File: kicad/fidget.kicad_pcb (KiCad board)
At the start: 2 copper layers, 74 x 38.9 mm, 13 parts, among them SW1 SW_Push, SW2 SW_Push, SW3 SW_Push, SW4 SW_Push, U1 XIAO-RP2040-DIP

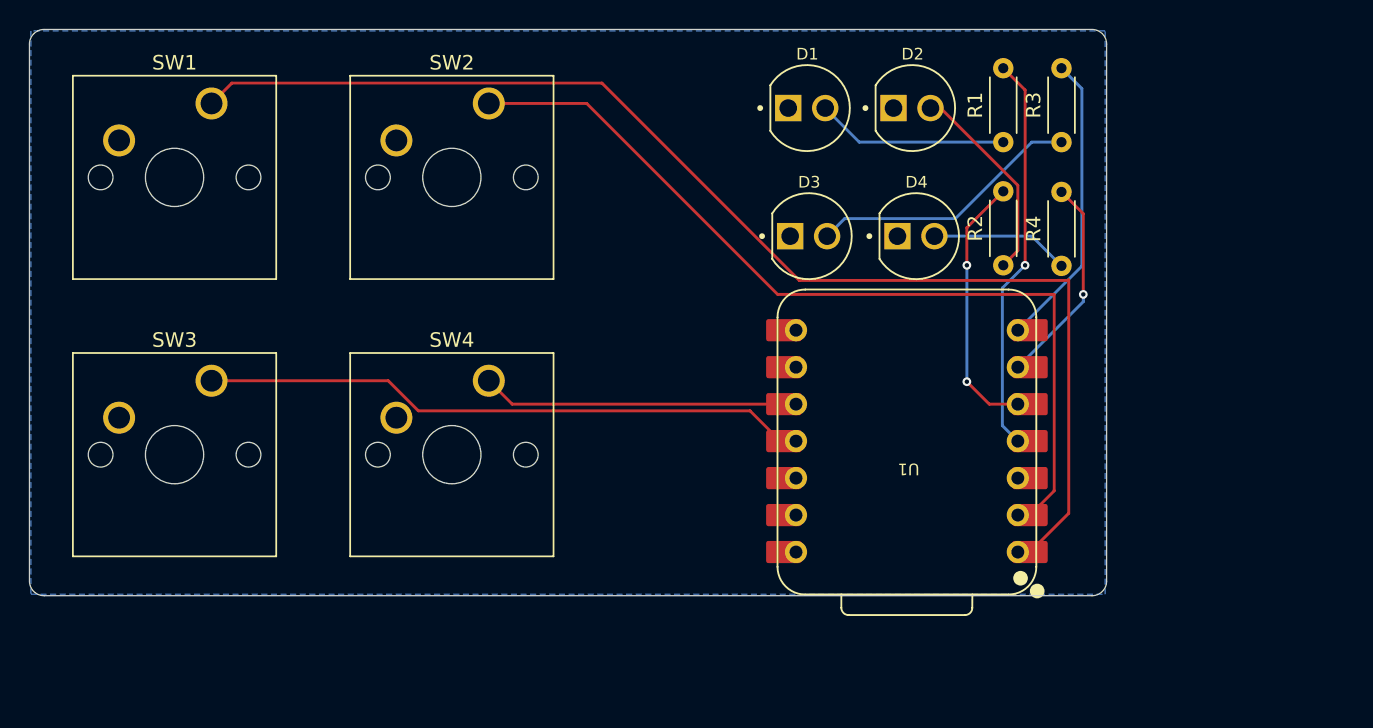
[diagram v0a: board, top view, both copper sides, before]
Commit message: update silkscreen + images
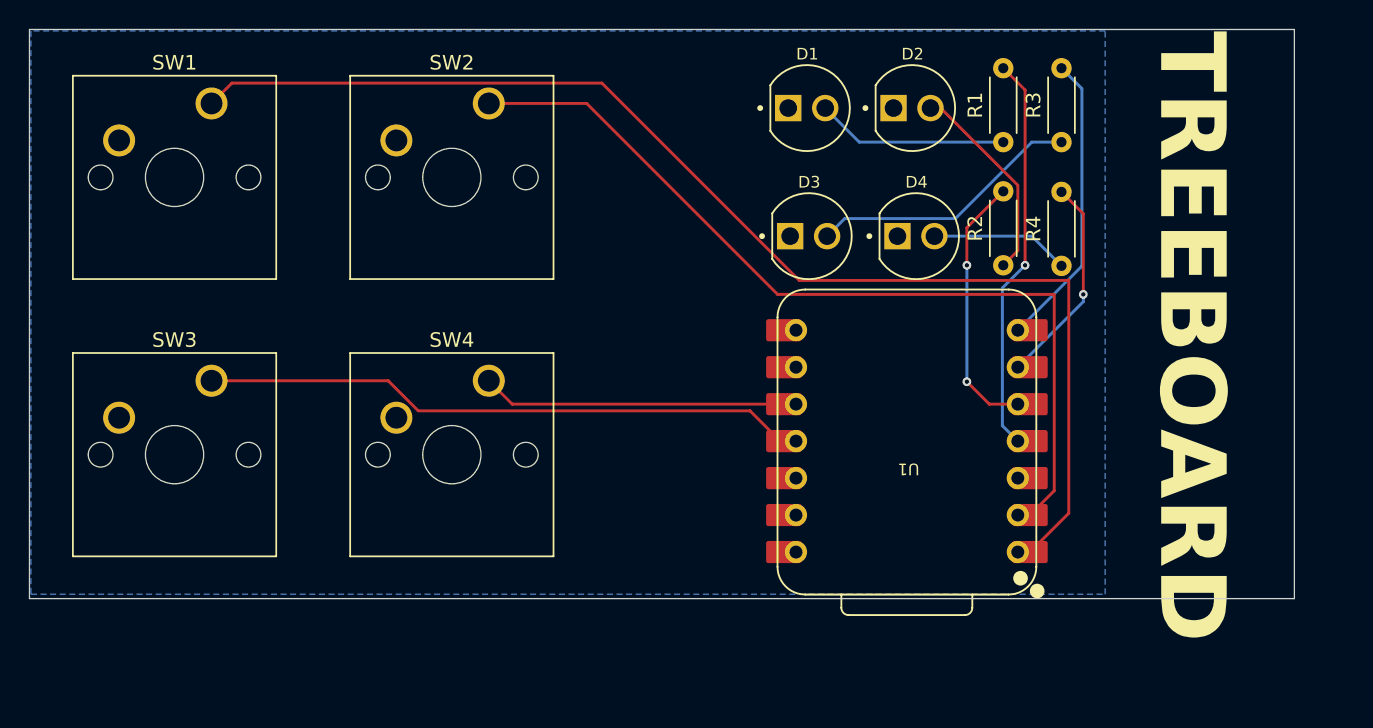
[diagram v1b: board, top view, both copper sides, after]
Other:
- board size 74 x 38.9 mm -> 86.9 x 39.1 mm
- board text added: "Duel"
- board text added: "GAMES"
- board text added: "Memory Game"
- board text added: "Reaction Tester"
- board text added: "TREEBOARD"
- board text added: "go to https://github.com/DaBlower/treeboard to view instructions"
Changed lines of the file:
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@@
 		)
 	)
-	(gr_arc
-		(start 85.6 71.8)
-		(mid 85.892893 71.092893)
-		(end 86.6 70.8)
+	(gr_rect
+		(start 85.6 70.8)
+		(end 172.5 109.9)
 		(stroke
 			(width 0.05)
 			(type default)
 		)
+		(fill none)
 		(layer "Edge.Cuts")
 	)
-	(gr_line
-		(start 158.6 109.7)
-		(end 86.6 109.7)
-		(stroke
-			(width 0.05)
-			(type default)
+	(gr_text "Reaction Tester"
+		(at 132.3 107.8 270)
+		(layer "B.SilkS")
+		(effects
+			(font
+				(size 3 3)
+				(thickness 0.6)
+				(bold yes)
+			)
+			(justify left bottom mirror)
 		)
-		(layer "Edge.Cuts")
 	)
-	(gr_arc
-		(start 159.6 108.7)
-		(mid 159.307107 109.407107)
-		(end 158.6 109.7)
-		(stroke
-			(width 0.05)
-			(type default)
+	(gr_text "Duel"
+		(at 128.2 107.8 270)
+		(layer "B.SilkS")
+		(effects
+			(font
+				(size 3 3)
+				(thickness 0.6)
+				(bold yes)
+			)
+			(justify left bottom mirror)
 		)
-		(layer "Edge.Cuts")
 	)
-	(gr_arc
-		(start 158.6 70.8)
-		(mid 159.307107 71.092893)
-		(end 159.6 71.8)
-		(stroke
-			(width 0.05)
-			(type default)
+	(gr_text "GAMES"
+		(at 161.4 108.5 270)
+		(layer "B.SilkS")
+		(effects
+			(font
+				(size 7 7)
+				(thickness 1.75)
+				(bold yes)
+			)
+			(justify left bottom mirror)
 		)
-		(layer "Edge.Cuts")
 	)
-	(gr_line
-		(start 159.6 71.8)
-		(end 159.6 108.7)
-		(stroke
-			(width 0.05)
-			(type default)
+	(gr_text "go to\nhttps://github.com/DaBlower/treeboard\nto view instructions"
+		(at 103.3 106.4 270)
+		(layer "B.SilkS")
+		(effects
+			(font
+				(size 1 1)
+				(thickness 0.2)
+				(bold yes)
+			)
+			(justify left bottom mirror)
 		)
-		(layer "Edge.Cuts")
 	)
-	(gr_line
-		(start 86.6 70.8)
-		(end 158.6 70.8)
-		(stroke
-			(width 0.05)
-			(type default)
+	(gr_text "Memory Game"
+		(at 124.2 107.8 270)
+		(layer "B.SilkS")
+		(effects
+			(font
+				(size 3 3)
+				(thickness 0.6)
+				(bold yes)
+			)
+			(justify left bottom mirror)
 		)
-		(layer "Edge.Cuts")
 	)
-	(gr_line
-		(start 85.6 108.7)
-		(end 85.6 71.8)
-		(stroke
-			(width 0.05)
-			(type default)
+	(gr_text "TREEBOARD"
+		(at 162.8 70.9 270)
+		(layer "F.SilkS")
+		(effects
+			(font
+				(size 4.5 4.5)
+				(thickness 1.125)
+				(bold yes)
+			)
+			(justify left bottom)
 		)
-		(layer "Edge.Cuts")
-	)
-	(gr_arc
-		(start 86.6 109.7)
-		(mid 85.892893 109.407107)
-		(end 85.6 108.7)
-		(stroke
-			(width 0.05)
-			(type default)
-		)
-		(layer "Edge.Cuts")
 	)
 	(segment

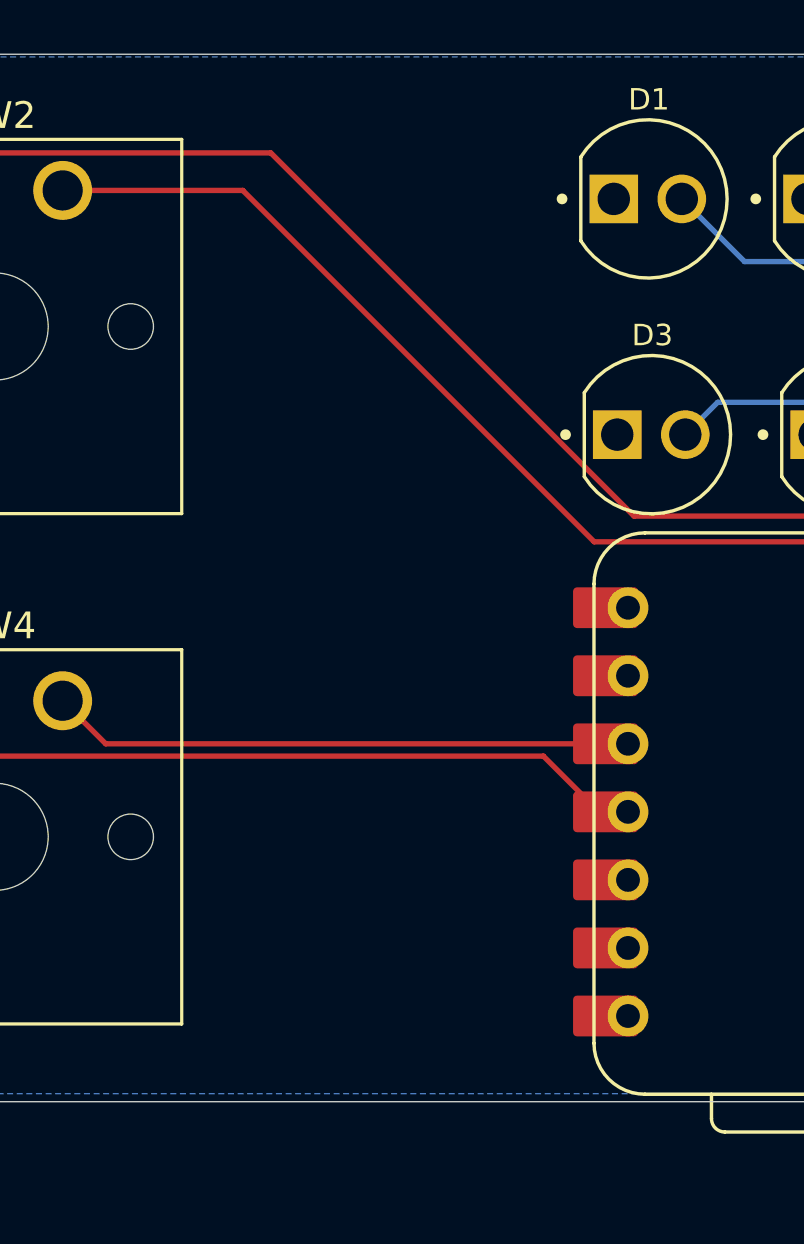
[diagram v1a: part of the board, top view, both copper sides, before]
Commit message: add more silkscreen
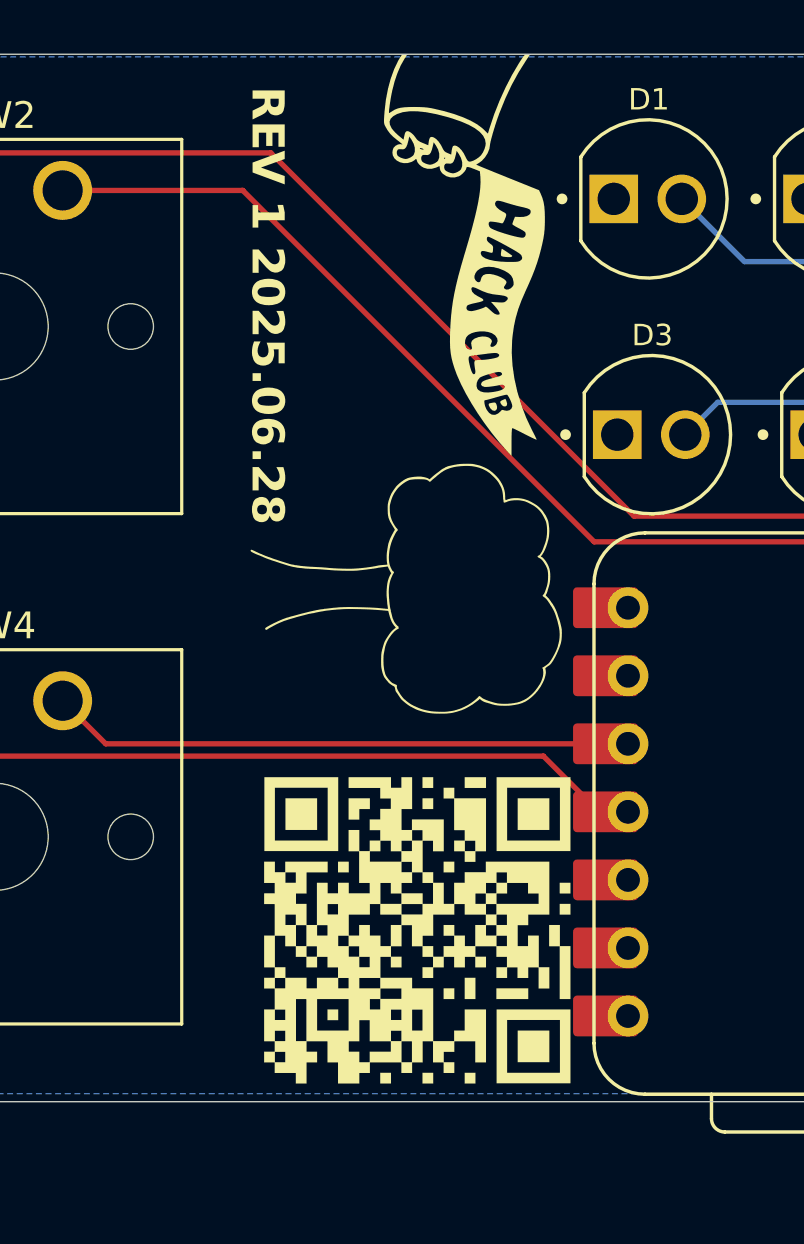
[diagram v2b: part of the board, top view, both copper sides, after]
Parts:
- added G***: LOGO, LOGO, F.Cu at (132.2, 78.3)
- added G***: LOGO, LOGO, F.Cu at (129.8, 90.9)
- added G***: LOGO, LOGO, F.Cu at (130.4, 103.5)
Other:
- board text added: "REV 1 2025.06.28"

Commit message: add keychain hole
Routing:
- net (no net): vias 0 -> 1
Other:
- board size 86.9 x 39.1 mm -> 90.3 x 39.1 mm
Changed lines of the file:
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@@
 			(plot_on_all_layers_selection 0x0000000_00000000)
 			(disableapertmacros no)
-			(usegerberextensions no)
+			(usegerberextensions yes)
 			(usegerberattributes yes)
 			(usegerberadvancedattributes yes)
@@
 			(plotinvisibletext no)
 			(sketchpadsonfab no)
-			(subtractmaskfromsilk no)
+			(subtractmaskfromsilk yes)
 			(outputformat 1)
 			(mirror no)
-			(drillshape 1)
+			(drillshape 0)
 			(scaleselection 1)
-			(outputdirectory "")
+			(outputdirectory "production/")
 		)
 	)
@@
 		)
 	)
-	(gr_rect
-		(start 85.6 70.8)
-		(end 172.5 109.9)
+	(gr_arc
+		(start 174.9 70.8)
+		(mid 175.607107 71.092893)
+		(end 175.9 71.8)
+		(stroke
+			(width 0.05)
+			(type default)
+		)
+		(layer "Edge.Cuts")
+	)
+	(gr_line
+		(start 175.334394 78.239173)
+		(end 170.565606 84.860827)
+		(stroke
+			(width 0.05)
+			(type default)
+		)
+		(layer "Edge.Cuts")
+	)
+	(gr_line
+		(start 169 109.9)
+		(end 148.4 109.9)
+		(stroke
+			(width 0.05)
+			(type default)
+		)
+		(layer "Edge.Cuts")
+	)
+	(gr_arc
+		(start 170 86.614031)
+		(mid 170.144901 85.69294)
+		(end 170.565606 84.860827)
+		(stroke
+			(width 0.05)
+			(type default)
+		)
+		(layer "Edge.Cuts")
+	)
+	(gr_arc
+		(start 175.9 76.485969)
+		(mid 175.755099 77.40706)
+		(end 175.334394 78.239173)
+		(stroke
+			(width 0.05)
+			(type default)
+		)
+		(layer "Edge.Cuts")
+	)
+	(gr_line
+		(start 148.4 109.9)
+		(end 86.6 109.9)
+		(stroke
+			(width 0.05)
+			(type default)
+		)
+		(layer "Edge.Cuts")
+	)
+	(gr_line
+		(start 175.9 71.8)
+		(end 175.9 76.485969)
+		(stroke
+			(width 0.05)
+			(type default)
+		)
+		(layer "Edge.Cuts")
+	)
+	(gr_arc
+		(start 86.6 109.9)
+		(mid 85.892893 109.607107)
+		(end 85.6 108.9)
+		(stroke
+			(width 0.05)
+			(type default)
+		)
+		(layer "Edge.Cuts")
+	)
+	(gr_line
+		(start 170 108.9)
+		(end 170 86.614031)
+		(stroke
+			(width 0.05)
+			(type default)
+		)
+		(layer "Edge.Cuts")
+	)
+	(gr_arc
+		(start 85.6 71.8)
+		(mid 85.892893 71.092893)
+		(end 86.6 70.8)
+		(stroke
+			(width 0.05)
+			(type default)
+		)
+		(layer "Edge.Cuts")
+	)
+	(gr_line
+		(start 86.6 70.8)
+		(end 174.9 70.8)
+		(stroke
+			(width 0.05)
+			(type default)
+		)
+		(layer "Edge.Cuts")
+	)
+	(gr_arc
+		(start 170 108.9)
+		(mid 169.707107 109.607107)
+		(end 169 109.9)
+		(stroke
+			(width 0.05)
+			(type default)
+		)
+		(layer "Edge.Cuts")
+	)
+	(gr_line
+		(start 85.6 108.9)
+		(end 85.6 71.8)
 		(stroke
 			(width 0.05)
 			(type default)
 		)
-		(fill none)
 		(layer "Edge.Cuts")
 	)
@@
 	)
 	(gr_text "GAMES"
-		(at 161.4 108.5 270)
+		(at 160.2 108.5 270)
 		(layer "B.SilkS")
 		(effects
@@
 	)
 	(gr_text "TREEBOARD"
-		(at 162.8 70.9 270)
+		(at 160.8 70.8 270)
 		(layer "F.SilkS")
 		(effects
@@
 		)
 	)
+	(via
+		(at 172.3 74.3)
+		(size 5.5)
+		(drill 5)
+		(layers "F.Cu" "B.Cu")
+		(net 0)
+	)
 	(segment
 		(start 142.61 78.54)
@@
 		(polygon
 			(pts
-				(xy 159.5 70.9) (xy 85.7 70.9) (xy 85.7 109.6) (xy 159.5 109.6)
+				(xy 159.5 70.9) (xy 86 71.4) (xy 86 109.5) (xy 159.5 109.6)
 			)
 		)

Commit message: update production files
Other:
- board text added: "Binary"
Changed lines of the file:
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@@
 		(layer "Edge.Cuts")
+	)
+	(gr_text "Binary"
+		(at 120.1 107.8 270)
+		(layer "B.SilkS")
+		(effects
+			(font
+				(size 3 3)
+				(thickness 0.6)
+				(bold yes)
+			)
+			(justify left bottom mirror)
+		)
 	)
 	(gr_text "Reaction Tester"
